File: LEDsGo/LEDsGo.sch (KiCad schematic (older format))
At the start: 20 parts, among them J1 AVR-ISP-6, J1 USB_B_Micro, U1 CH340G, U2 ATmega328P-AU, Y1 12MHz, Y2 12MHz

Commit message: Updated schematic.
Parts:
- removed R1, R2: 10k, symbol Device:R_Small_US
- added C10, C11: 100nF, Capacitor_SMD:C_0805_2012Metric, symbol Device:C_Small
- added C8, C9: 1uF, Capacitor_SMD:C_0805_2012Metric, symbol Device:C_Small
- added DS1: HY1602E, Display:HY1602E, symbol Display_Character:HY1602E
- added RV1: 10k, symbol Device:R_POT_TRIM_US
- added U3: NCV8114ASN330T1G, Package_TO_SOT_SMD:TSOT-23-5, symbol Regulator_Linear:NCV8114ASN330T1G
- C1, C2, C3, C4, C5, C6, C7: footprint (none) -> Capacitor_SMD:C_0805_2012Metric
- D1, D2: footprint (none) -> LED_SMD:LED_0805_2012Metric
- J1: footprint (none) -> Connector_USB:USB_Micro-B_Molex_47346-0001
- J2: renamed from J1; footprint (none) -> Connector_PinHeader_1.27mm:PinHeader_2x03_P1.27mm_Vertical
- R1: renamed from R3; footprint (none) -> Resistor_SMD:R_0805_2012Metric
- R2: renamed from R4; footprint (none) -> Resistor_SMD:R_0805_2012Metric
- R3: renamed from R5; footprint (none) -> Resistor_SMD:R_0805_2012Metric
- Y1, Y2: footprint (none) -> Crystal:Crystal_HC49-4H_Vertical
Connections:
- net +5V: now also R1.1, R2.1, C10.2, C8.1, DS1.2 (LEDA), DS1.4 (VDD), RV1.3, U3.1 (IN), U3.3 (EN); no longer C3.1, U1.16 (VCC)
- net GND: now also C6.1, J1.6 (Shield), C10.1, C8.2, C9.2, DS1.1 (LEDK), DS1.3 (VSS), RV1.1, U3.2 (GND); no longer R1.1, R2.1, Y2.1
- net RST: now also C11.1
- net RX: now also D1.1 (K); no longer D1.2 (A)
- net TX: now also D2.1 (K); no longer D2.2 (A)
- net PD3: now reaches U2.1 (PD3)
- net PD3: now also DS1.14 (DB5)
- net PB0: now reaches U2.12 (PB0)
- net PB0: now also DS1.8 (E)
- net PB1: now reaches U2.13 (PB1)
- net PB1: now also DS1.7 (R/~W)
- net PB2: now reaches U2.14 (PB2)
- net PB2: now also DS1.6 (RS)
- net PD4: now reaches U2.2 (PD4)
- net PD4: now also DS1.15 (DB6)
- net PD2: now reaches U2.32 (PD2)
- net PD2: now also DS1.13 (DB4)
- net at C5.1, U2.7 (XTAL1/PB6): now also Y2.1
- net at C6.2, U2.8 (XTAL2/PB7): now also Y2.2
- net PD5: now reaches U2.9 (PD5)
- net PD5: now also DS1.16 (DB7)
- net at U1.14 (~RTS): now also C11.2
- net +3V3: now reaches C4.1, U1.4 (V3)
- net +3V3: now also C3.1, U1.16 (VCC), C9.1, U3.5 (OUT)
- net at R1.2: now also D1.2 (A); no longer D1.1 (K)
- net at R2.2: now also D2.2 (A); no longer D2.1 (K)
- new net: DS1.5 (Vo), RV1.2
- no-connect marks 0 -> 22
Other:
- note removed: "9/13/2020"
- moved on the sheet: C1, C2, C3, C4, C5, C6, C7, D1, D2, J2, R1, R2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

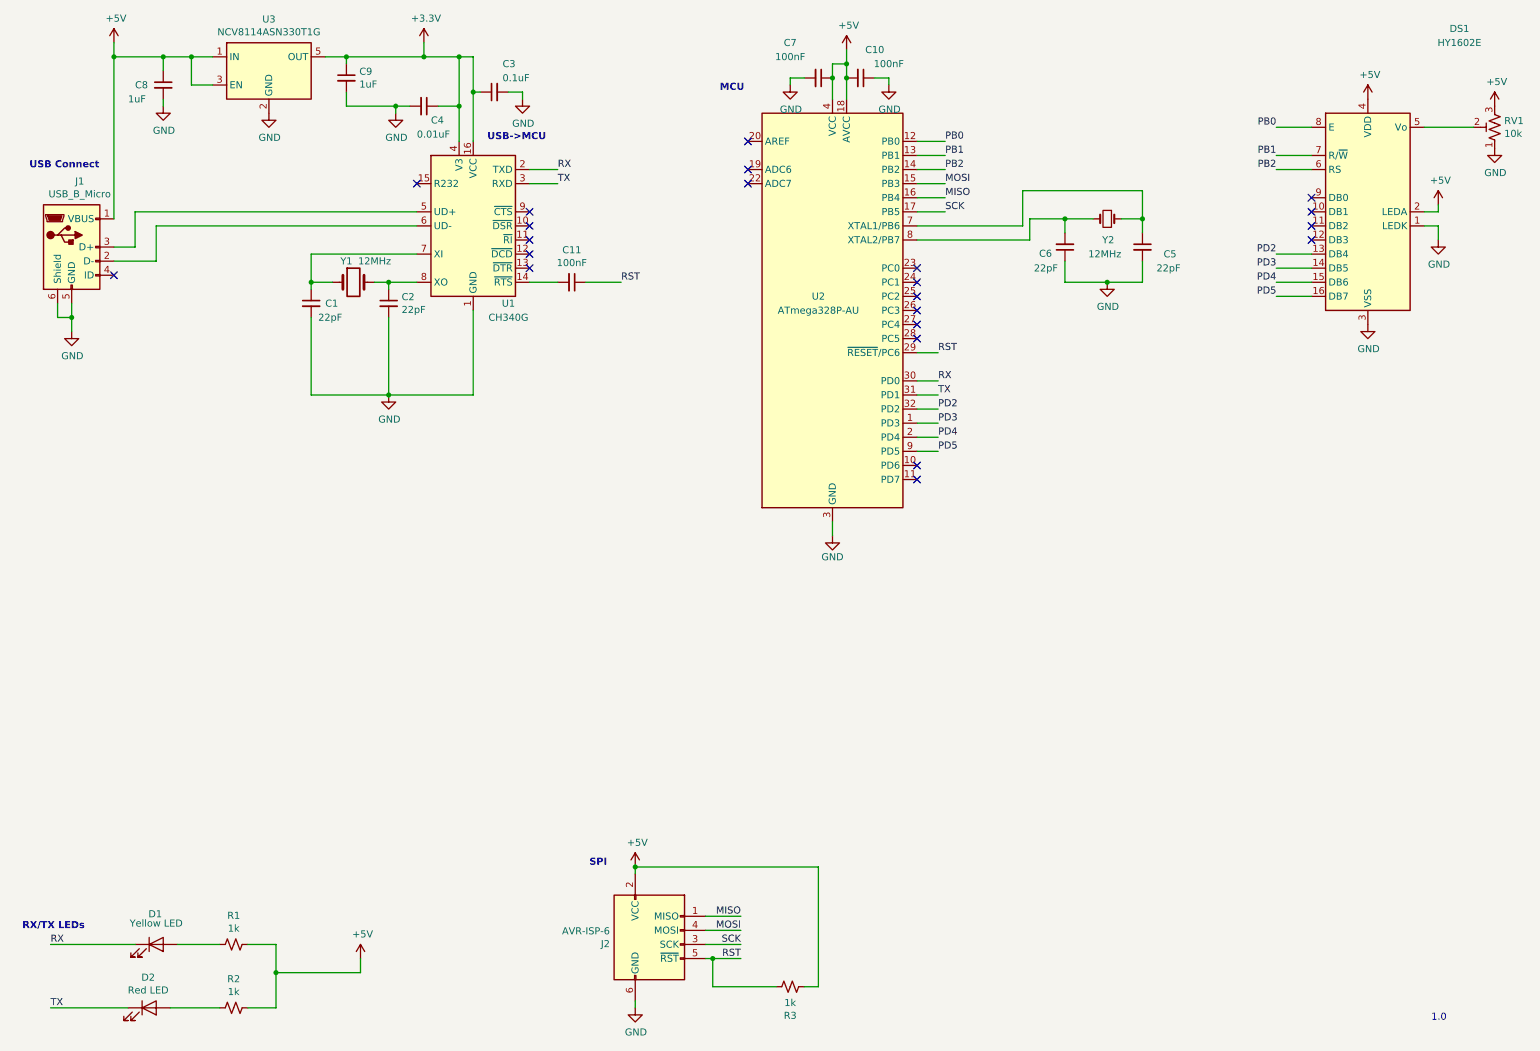
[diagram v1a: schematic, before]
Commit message: Added LCD switch capability, as well as switches/LED input to PC pins.
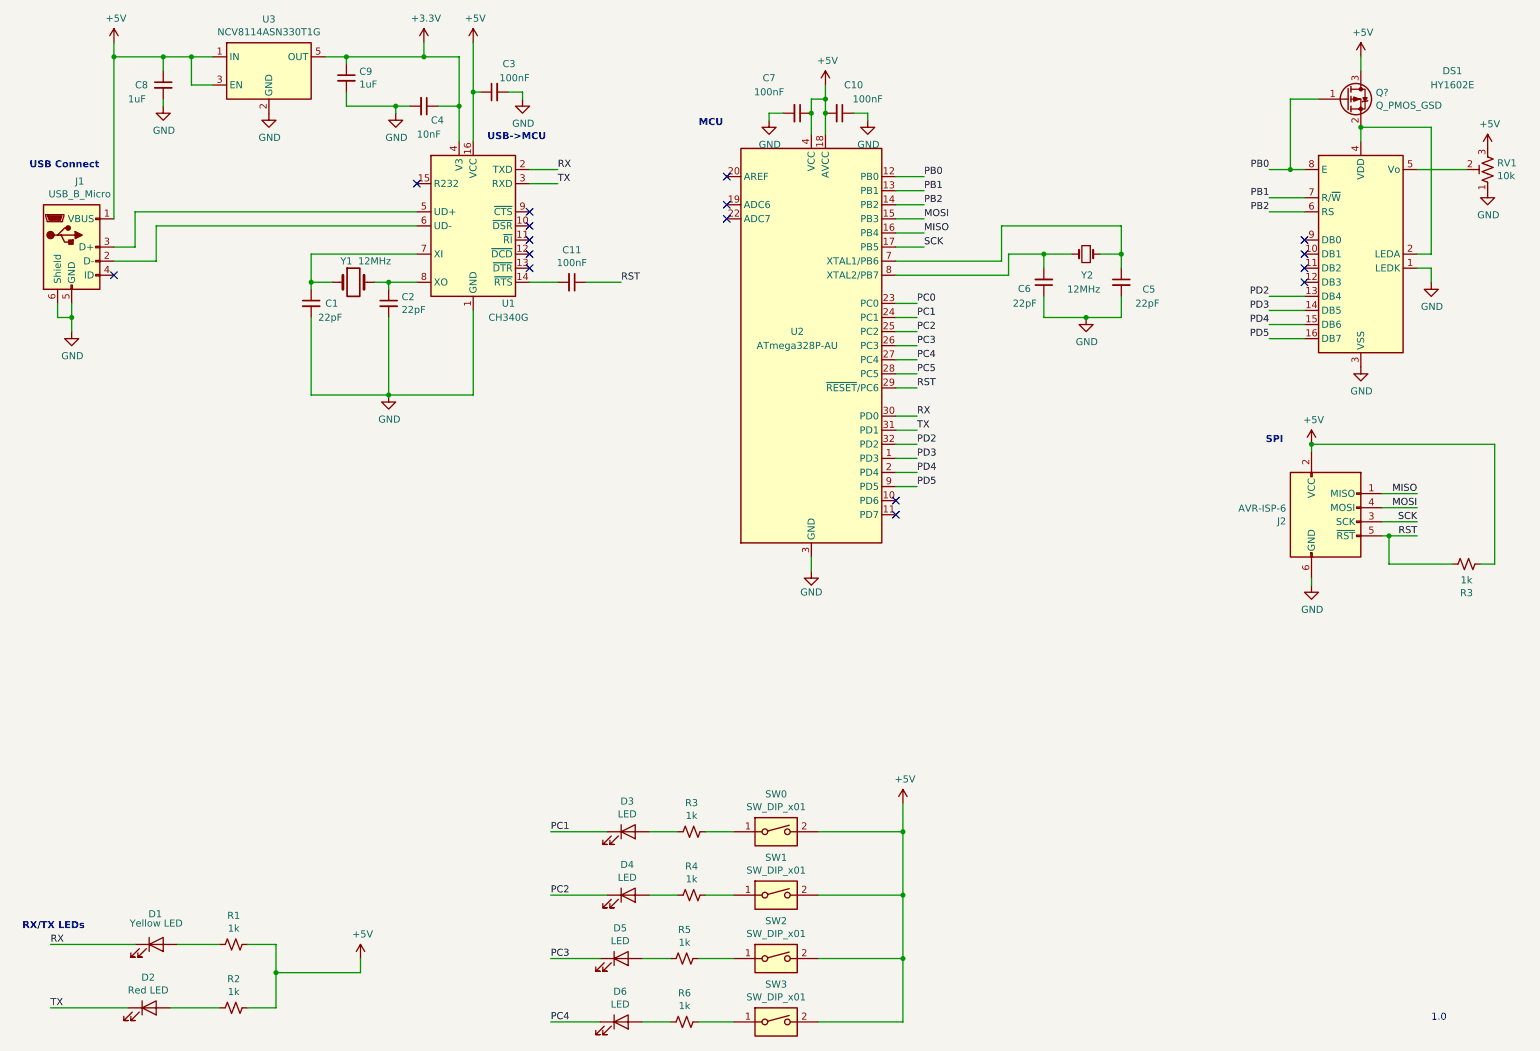
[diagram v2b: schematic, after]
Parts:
- added D3, D4, D5, D6: LED, symbol Device:LED
- added Q?: Q_PMOS_GSD, symbol Device:Q_PMOS_GSD
- added R3, R4, R5, R6: 1k, symbol Device:R_Small_US
- added SW0, SW1, SW2, SW3: SW_DIP_x01, symbol Switch:SW_DIP_x01
- C3: value 0.1uF -> 100nF
- C4: value 0.01uF -> 10nF
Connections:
- net +3V3: no longer C3.1, U1.16 (VCC)
- net +5V: now also C3.1, U1.16 (VCC), Q?.3 (D), SW0.2, SW1.2, SW2.2, SW3.2; no longer DS1.2 (LEDA), DS1.4 (VDD)
- net PB0: now also Q?.1 (G)
- net PC0: now reaches U2.23 (PC0)
- net PC1: now reaches U2.24 (PC1)
- net PC1: now also D3.1 (K)
- net PC2: now reaches U2.25 (PC2)
- net PC2: now also D4.1 (K)
- net PC3: now reaches U2.26 (PC3)
- net PC3: now also D5.1 (K)
- net PC4: now reaches U2.27 (PC4)
- net PC4: now also D6.1 (K)
- net PC5: now reaches U2.28 (PC5)
- new net: DS1.2 (LEDA), DS1.4 (VDD), Q?.2 (S)
- new net: R3.1, SW0.1
- new net: R4.1, SW1.1
- new net: R5.1, SW2.1
- new net: R6.1, SW3.1
- new net: D3.2 (A), R3.2
- new net: D4.2 (A), R4.2
- new net: D5.2 (A), R5.2
- new net: D6.2 (A), R6.2
- no-connect marks 22 -> 16
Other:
- moved on the sheet: C10, C5, C6, C7, DS1, J2, R3, RV1, U2, Y2

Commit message: Implemented some button inputs and updated text.
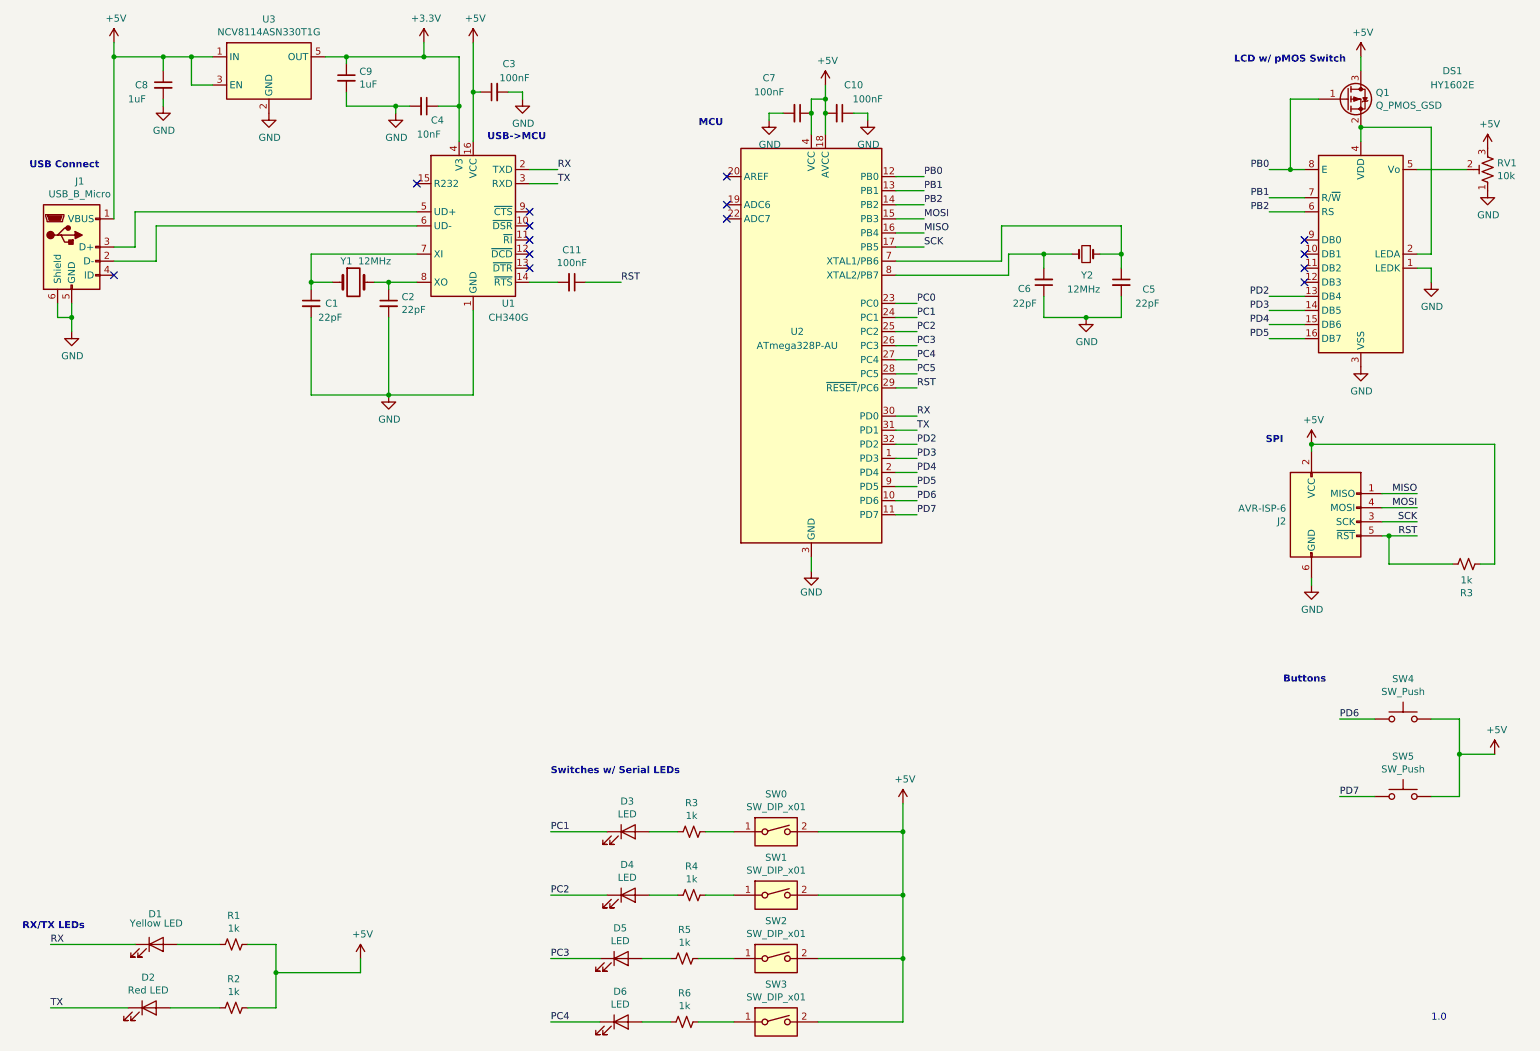
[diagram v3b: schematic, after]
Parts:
- added SW4, SW5: SW_Push, symbol Switch:SW_Push
- gave numbers to parts that had none: 1
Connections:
- net +5V: now also SW4.2, SW5.2
- net PD6: now reaches U2.10 (PD6)
- net PD6: now also SW4.1
- net PD7: now reaches U2.11 (PD7)
- net PD7: now also SW5.1
- no-connect marks 16 -> 14
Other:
- note added: "Buttons"
- note added: "LCD w/ pMOS Switch"
- note added: "Switches w/ Serial LEDs"
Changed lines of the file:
@@
 	1    0    0    -1
 $EndComp
-NoConn ~ 6750 3950
-NoConn ~ 6750 4050
 $Comp
 L MCU_Microchip_ATmega:ATmega328P-AU U2
@@
 Connection ~ 3750 1050
 $Comp
-L Device:Q_PMOS_GSD Q?
+L Device:Q_PMOS_GSD Q1
 U 1 1 5F6C9B76
 P 9950 1100
-F 0 "Q?" H 10156 1146 50  0000 L CNN
+F 0 "Q1" H 10156 1146 50  0000 L CNN
 F 1 "Q_PMOS_GSD" H 10156 1055 50  0000 L CNN
 F 2 "" H 10150 1200 50  0001 C CNN
@@
 Wire Wire Line
 	6750 3050 6900 3050
+$Comp
+L Switch:SW_Push SW4
+U 1 1 5F6D9037
+P 10350 5500
+F 0 "SW4" H 10350 5785 50  0000 C CNN
+F 1 "SW_Push" H 10350 5694 50  0000 C CNN
+F 2 "" H 10350 5700 50  0001 C CNN
+F 3 "~" H 10350 5700 50  0001 C CNN
+	1    10350 5500
+	1    0    0    -1
+$EndComp
+$Comp
+L Switch:SW_Push SW5
+U 1 1 5F6DB122
+P 10350 6050
+F 0 "SW5" H 10350 6335 50  0000 C CNN
+F 1 "SW_Push" H 10350 6244 50  0000 C CNN
+F 2 "" H 10350 6250 50  0001 C CNN
+F 3 "~" H 10350 6250 50  0001 C CNN
+	1    10350 6050
+	1    0    0    -1
+$EndComp
+$Comp
+L power:+5V #PWR?
+U 1 1 5F6E43C0
+P 11000 5750
+F 0 "#PWR?" H 11000 5600 50  0001 C CNN
+F 1 "+5V" H 11015 5923 50  0000 C CNN
+F 2 "" H 11000 5750 50  0001 C CNN
+F 3 "" H 11000 5750 50  0001 C CNN
+	1    11000 5750
+	1    0    0    -1
+$EndComp
+Wire Wire Line
+	10550 5500 10750 5500
+Wire Wire Line
+	10750 5500 10750 5750
+Wire Wire Line
+	10750 6050 10550 6050
+Wire Wire Line
+	10750 5750 11000 5750
+Connection ~ 10750 5750
+Wire Wire Line
+	10750 5750 10750 6050
+Text Label 6900 3950 0    50   ~ 0
+PD6
+Text Label 6900 4050 0    50   ~ 0
+PD7
+Wire Wire Line
+	6750 3950 6900 3950
+Wire Wire Line
+	6750 4050 6900 4050
+Text Label 9900 5500 0    50   ~ 0
+PD6
+Text Label 9900 6050 0    50   ~ 0
+PD7
+Wire Wire Line
+	9900 5500 10150 5500
+Wire Wire Line
+	9900 6050 10150 6050
+Text Notes 9500 5250 0    50   ~ 10
+Buttons
+Text Notes 4300 5900 0    50   ~ 10
+Switches w/ Serial LEDs
+Text Notes 9150 850  0    50   ~ 10
+LCD w/ pMOS Switch
 $EndSCHEMATC

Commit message: Removed LCD to incorporate more buttons. Adjusted LEDs to be output and switches to be inputs.
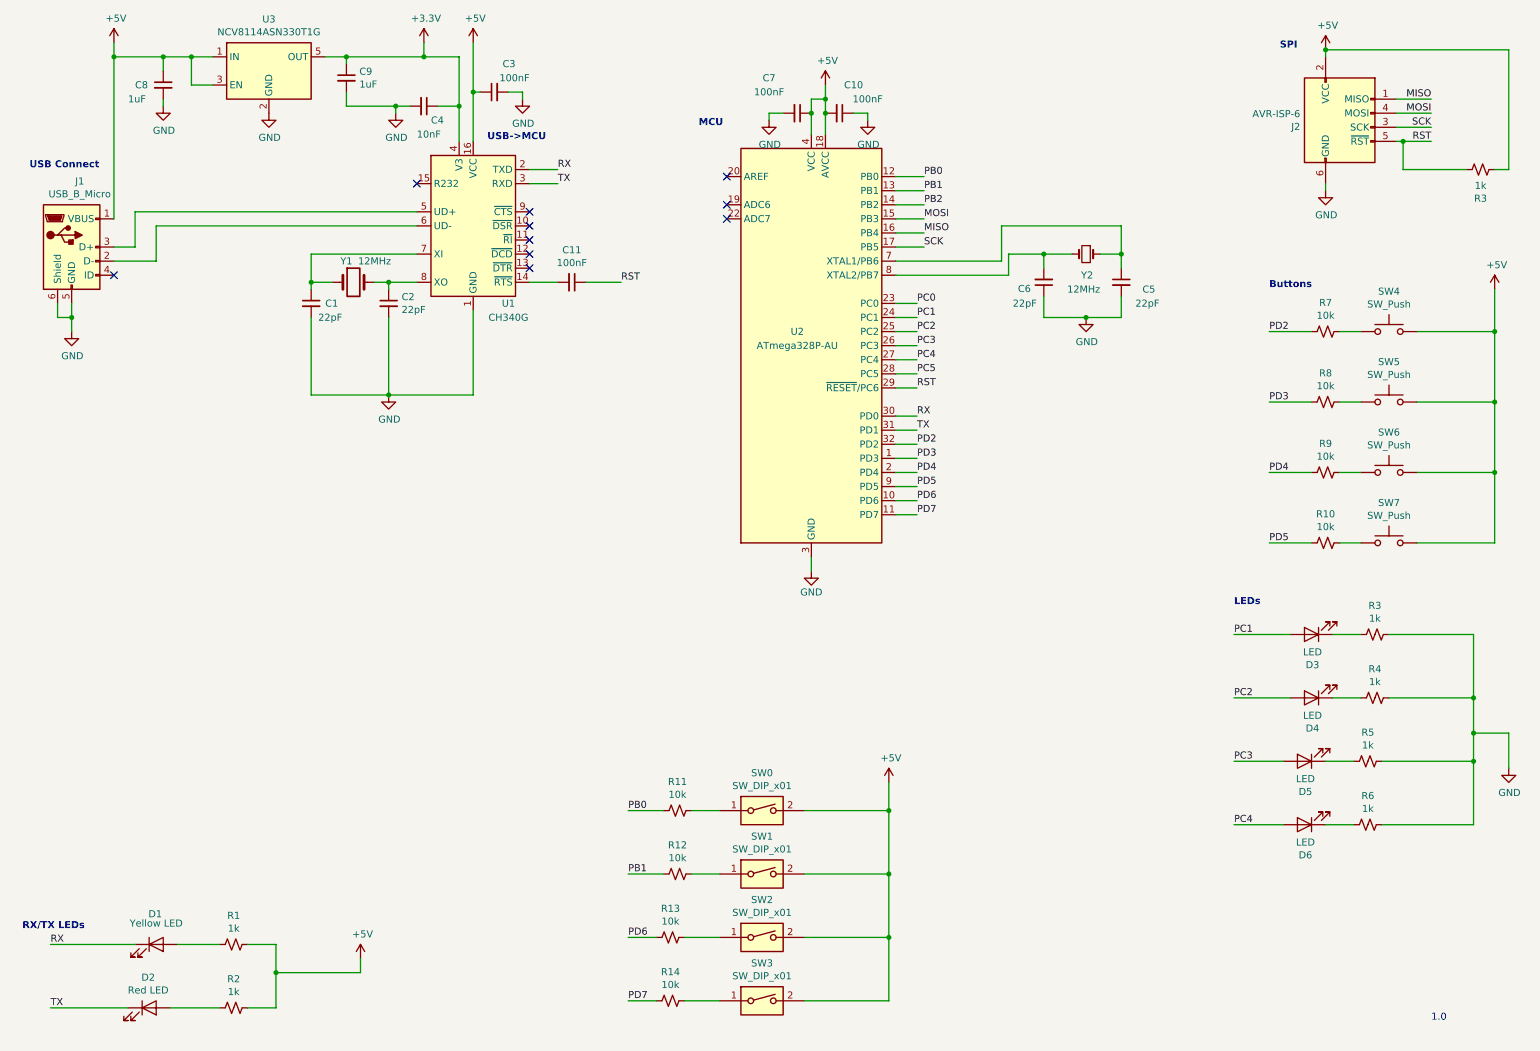
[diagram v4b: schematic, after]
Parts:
- removed DS1: HY1602E, Display:HY1602E, symbol Display_Character:HY1602E
- removed Q1: Q_PMOS_GSD, symbol Device:Q_PMOS_GSD
- removed RV1: 10k, symbol Device:R_POT_TRIM_US
- added R10, R11, R12, R13, R14, R7, R8, R9: 10k, symbol Device:R_Small_US
- added SW6, SW7: SW_Push, symbol Switch:SW_Push
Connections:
- net +5V: now also SW6.2, SW7.2
- net GND: now also R3.1, R4.1, R5.1, R6.1
- net PB0: now also R11.2
- net PB1: now also R12.2
- net PC1: now also D3.2 (A); no longer D3.1 (K)
- net PC2: now also D4.2 (A); no longer D4.1 (K)
- net PC3: now also D5.2 (A); no longer D5.1 (K)
- net PC4: now also D6.2 (A); no longer D6.1 (K)
- net PD2: now also R7.2
- net PD3: now also R8.2
- net PD4: now also R9.2
- net PD5: now also R10.2
- net PD6: now also R13.2; no longer SW4.1
- net PD7: now also R14.2; no longer SW5.1
- net at SW0.1: now also R11.1; no longer R3.1
- net at SW1.1: now also R12.1; no longer R4.1
- net at SW2.1: now also R13.1; no longer R5.1
- net at SW3.1: now also R14.1; no longer R6.1
- net at R3.2: now also D3.1 (K); no longer D3.2 (A)
- net at R4.2: now also D4.1 (K); no longer D4.2 (A)
- net at R5.2: now also D5.1 (K); no longer D5.2 (A)
- net at R6.2: now also D6.1 (K); no longer D6.2 (A)
- new net: R7.1, SW4.1
- new net: R8.1, SW5.1
- new net: R9.1, SW6.1
- new net: R10.1, SW7.1
- no-connect marks 14 -> 10
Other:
- note added: "LEDs"
- note removed: "LCD w/ pMOS Switch"
- note removed: "Switches w/ Serial LEDs"
- moved on the sheet: D3, D4, D5, D6, J2, R3, R4, R5, R6, SW0, SW1, SW2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
